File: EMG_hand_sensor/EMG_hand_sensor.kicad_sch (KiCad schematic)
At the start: 42 parts, among them J1 USB_C_Receptacle_USB2.0_16P, J2 Conn_01x04_Pin, SW1 SW_SPDT, U1 USBLC6-2SC6, U10 TRS_AUDIO_JACK_3.5mm, U11 TRS_AUDIO_JACK_3.5mm, U2 STM32F103C8Tx, U3 INA128, U4 TRS_AUDIO_JACK_3.5mm, U5 INA128, U6 INA128, U7 LT1762, U8 TRS_AUDIO_JACK_3.5mm, U9 INA128, Y1 16MHz

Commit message: new schematic done
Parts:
- C1, C12, C13, C14, C15, C2, C3, C4, C5, C6, C7, C8: footprint (none) -> Capacitor_SMD:C_0805_2012Metric_Pad1.18x1.45mm_HandSolder
- D1: footprint (none) -> Diode_SMD:D_0805_2012Metric
- FB1, R1, R10, R2, R3, R4, R5, R6, R7, R8, R9: footprint (none) -> Resistor_SMD:R_0805_2012Metric_Pad1.20x1.40mm_HandSolder
- J1: footprint (none) -> Connector_Molex:Molex_CLIK-Mate_502386-0970_1x09-1MP_P1.25mm_Horizontal
- J2: footprint (none) -> Connector_PinHeader_2.54mm:PinHeader_1x04_P2.54mm_Vertical
- SW1: footprint (none) -> Relay_THT:Relay_SPDT_Omron_G6E
- U3, U5, U6, U9: footprint (none) -> INA:SOIC127P600X175-8N
- Y1: footprint (none) -> Crystal:Crystal_SMD_3225-4Pin_3.2x2.5mm
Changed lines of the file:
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@@
 			)
 		)
-		(property "Footprint" ""
+		(property "Footprint" "Capacitor_SMD:C_0805_2012Metric_Pad1.18x1.45mm_HandSolder"
 			(at 48.26 64.77 0)
 			(effects
@@
 			)
 		)
-		(property "Footprint" ""
+		(property "Footprint" "Capacitor_SMD:C_0805_2012Metric_Pad1.18x1.45mm_HandSolder"
 			(at 125.73 62.23 0)
 			(effects
@@
 			)
 		)
-		(property "Footprint" ""
+		(property "Footprint" "INA:SOIC127P600X175-8N"
 			(at 160.02 30.48 0)
 			(effects
@@
 			)
 		)
-		(property "Footprint" ""
+		(property "Footprint" "Resistor_SMD:R_0805_2012Metric_Pad1.20x1.40mm_HandSolder"
 			(at 112.522 30.48 90)
 			(effects
@@
 			)
 		)
-		(property "Footprint" ""
+		(property "Footprint" "Capacitor_SMD:C_0805_2012Metric_Pad1.18x1.45mm_HandSolder"
 			(at 113.03 62.23 0)
 			(effects
@@
 			)
 		)
-		(property "Footprint" ""
+		(property "Footprint" "Relay_THT:Relay_SPDT_Omron_G6E"
 			(at 40.64 92.71 0)
 			(effects
@@
 			)
 		)
-		(property "Footprint" ""
+		(property "Footprint" "Crystal:Crystal_SMD_3225-4Pin_3.2x2.5mm"
 			(at 41.91 130.81 0)
 			(effects
@@
 			)
 		)
-		(property "Footprint" ""
+		(property "Footprint" "Capacitor_SMD:C_0805_2012Metric_Pad1.18x1.45mm_HandSolder"
 			(at 68.58 64.77 0)
 			(effects
@@
 			)
 		)
-		(property "Footprint" ""
+		(property "Footprint" "Capacitor_SMD:C_0805_2012Metric_Pad1.18x1.45mm_HandSolder"
 			(at 54.61 81.28 0)
 			(effects
@@
 			)
 		)
-		(property "Footprint" ""
+		(property "Footprint" "Resistor_SMD:R_0805_2012Metric_Pad1.20x1.40mm_HandSolder"
 			(at 129.032 165.1 90)
 			(effects
@@
 			)
 		)
-		(property "Footprint" ""
+		(property "Footprint" "Resistor_SMD:R_0805_2012Metric_Pad1.20x1.40mm_HandSolder"
 			(at 217.932 138.43 90)
 			(effects
@@
 			)
 		)
-		(property "Footprint" ""
+		(property "Footprint" "Resistor_SMD:R_0805_2012Metric_Pad1.20x1.40mm_HandSolder"
 			(at 272.542 105.41 90)
 			(effects
@@
 			)
 		)
-		(property "Footprint" ""
+		(property "Footprint" "INA:SOIC127P600X175-8N"
 			(at 158.75 57.15 0)
 			(effects
@@
 			)
 		)
-		(property "Footprint" ""
+		(property "Footprint" "Resistor_SMD:R_0805_2012Metric_Pad1.20x1.40mm_HandSolder"
 			(at 134.62 57.912 90)
 			(effects
@@
 			)
 		)
-		(property "Footprint" ""
+		(property "Footprint" "Diode_SMD:D_0805_2012Metric"
 			(at 267.97 101.6 0)
 			(effects
@@
 			)
 		)
-		(property "Footprint" ""
+		(property "Footprint" "Resistor_SMD:R_0805_2012Metric_Pad1.20x1.40mm_HandSolder"
 			(at 217.932 129.54 90)
 			(effects
@@
 			)
 		)
-		(property "Footprint" ""
+		(property "Footprint" "Capacitor_SMD:C_0805_2012Metric_Pad1.18x1.45mm_HandSolder"
 			(at 54.61 64.77 0)
 			(effects
@@
 			)
 		)
-		(property "Footprint" ""
+		(property "Footprint" "INA:SOIC127P600X175-8N"
 			(at 101.6 30.48 0)
 			(effects
@@
 			)
 		)
-		(property "Footprint" ""
+		(property "Footprint" "Capacitor_SMD:C_0805_2012Metric_Pad1.18x1.45mm_HandSolder"
 			(at 139.7 62.23 0)
 			(effects
@@
 			)
 		)
-		(property "Footprint" ""
+		(property "Footprint" "Connector_PinHeader_2.54mm:PinHeader_1x04_P2.54mm_Vertical"
 			(at 143.51 113.03 0)
 			(effects
@@
 			)
 		)
-		(property "Footprint" ""
+		(property "Footprint" "Resistor_SMD:R_0805_2012Metric_Pad1.20x1.40mm_HandSolder"
 			(at 169.672 57.15 90)
 			(effects
@@
 			)
 		)
-		(property "Footprint" ""
+		(property "Footprint" "Resistor_SMD:R_0805_2012Metric_Pad1.20x1.40mm_HandSolder"
 			(at 172.212 87.63 90)
 			(effects
@@
 			)
 		)
-		(property "Footprint" ""
+		(property "Footprint" "Connector_Molex:Molex_CLIK-Mate_502386-0970_1x09-1MP_P1.25mm_Horizontal"
 			(at 153.67 144.78 0)
 			(effects
@@
 			)
 		)
-		(property "Footprint" ""
+		(property "Footprint" "INA:SOIC127P600X175-8N"
 			(at 161.29 87.63 0)
 			(effects
@@
 			)
 		)
-		(property "Footprint" ""
+		(property "Footprint" "Resistor_SMD:R_0805_2012Metric_Pad1.20x1.40mm_HandSolder"
 			(at 135.382 165.1 90)
 			(effects
@@
 			)
 		)
-		(property "Footprint" ""
+		(property "Footprint" "Resistor_SMD:R_0805_2012Metric_Pad1.20x1.40mm_HandSolder"
 			(at 53.34 94.488 90)
 			(effects
@@
 			)
 		)
-		(property "Footprint" ""
+		(property "Footprint" "Capacitor_SMD:C_0805_2012Metric_Pad1.18x1.45mm_HandSolder"
 			(at 62.23 64.77 0)
 			(effects
@@
 			)
 		)
-		(property "Footprint" ""
+		(property "Footprint" "Resistor_SMD:R_0805_2012Metric_Pad1.20x1.40mm_HandSolder"
 			(at 170.942 30.48 90)
 			(effects
@@
 			)
 		)
-		(property "Footprint" ""
+		(property "Footprint" "Capacitor_SMD:C_0805_2012Metric_Pad1.18x1.45mm_HandSolder"
 			(at 39.37 64.77 0)
 			(effects
@@
 			)
 		)
-		(property "Footprint" ""
+		(property "Footprint" "Capacitor_SMD:C_0805_2012Metric_Pad1.18x1.45mm_HandSolder"
 			(at 74.93 64.77 0)
 			(effects
@@
 			)
 		)
-		(property "Footprint" ""
+		(property "Footprint" "Capacitor_SMD:C_0805_2012Metric_Pad1.18x1.45mm_HandSolder"
 			(at 53.34 135.89 0)
 			(effects
@@
 			)
 		)
-		(property "Footprint" ""
+		(property "Footprint" "Capacitor_SMD:C_0805_2012Metric_Pad1.18x1.45mm_HandSolder"
 			(at 29.21 137.16 0)
 			(effects

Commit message: starting pch layout
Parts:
- removed U10, U11, U4, U8: TRS_AUDIO_JACK_3.5mm, Connector_Audio:Jack_3.5mm_CUI_SJ-3523-SMT_Horizontal, symbol Audio_connector:TRS_connn
- added J3, J4, J5, J6: AudioJack3, Connector_Audio:Jack_3.5mm_CUI_SJ-3523-SMT_Horizontal, symbol Connector_Audio:AudioJack3
- J1: footprint Connector_Molex:Molex_CLIK-Mate_502386-0970_1x09-1MP_P1.25mm_Horizontal -> Connector_USB:USB_C_Receptacle_GCT_USB4105-xx-A_16P_TopMnt_Horizontal
- SW1: footprint Relay_THT:Relay_SPDT_Omron_G6E -> Button_Switch_SMD:SW_SPDT_CK_JS102011SAQN
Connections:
- net E1: now also J5.R; no longer U2.10 (PA0), U2.13 (PA3), U3.6
- net E2: now also J5.T
- net E3: now also J3.T; no longer U2.12 (PA2), U6.6
- net E4: now also J3.R; no longer U2.11 (PA1), U5.6, U9.6
- net E5: now also J6.R; no longer U5.3 (+)
- net E6: now also J6.T; no longer U5.2 (-)
- net E7: now also U5.3 (+), J4.T
- net E8: now also U5.2 (-), J4.R
- net GND: now also J3.S, J4.S, J5.S, J6.S
- new net O1: U2.10 (PA0), U6.6
- new net O2: U2.11 (PA1), U9.6
- new net O3: U2.12 (PA2), U5.6
- new net O4: U2.13 (PA3), U3.6

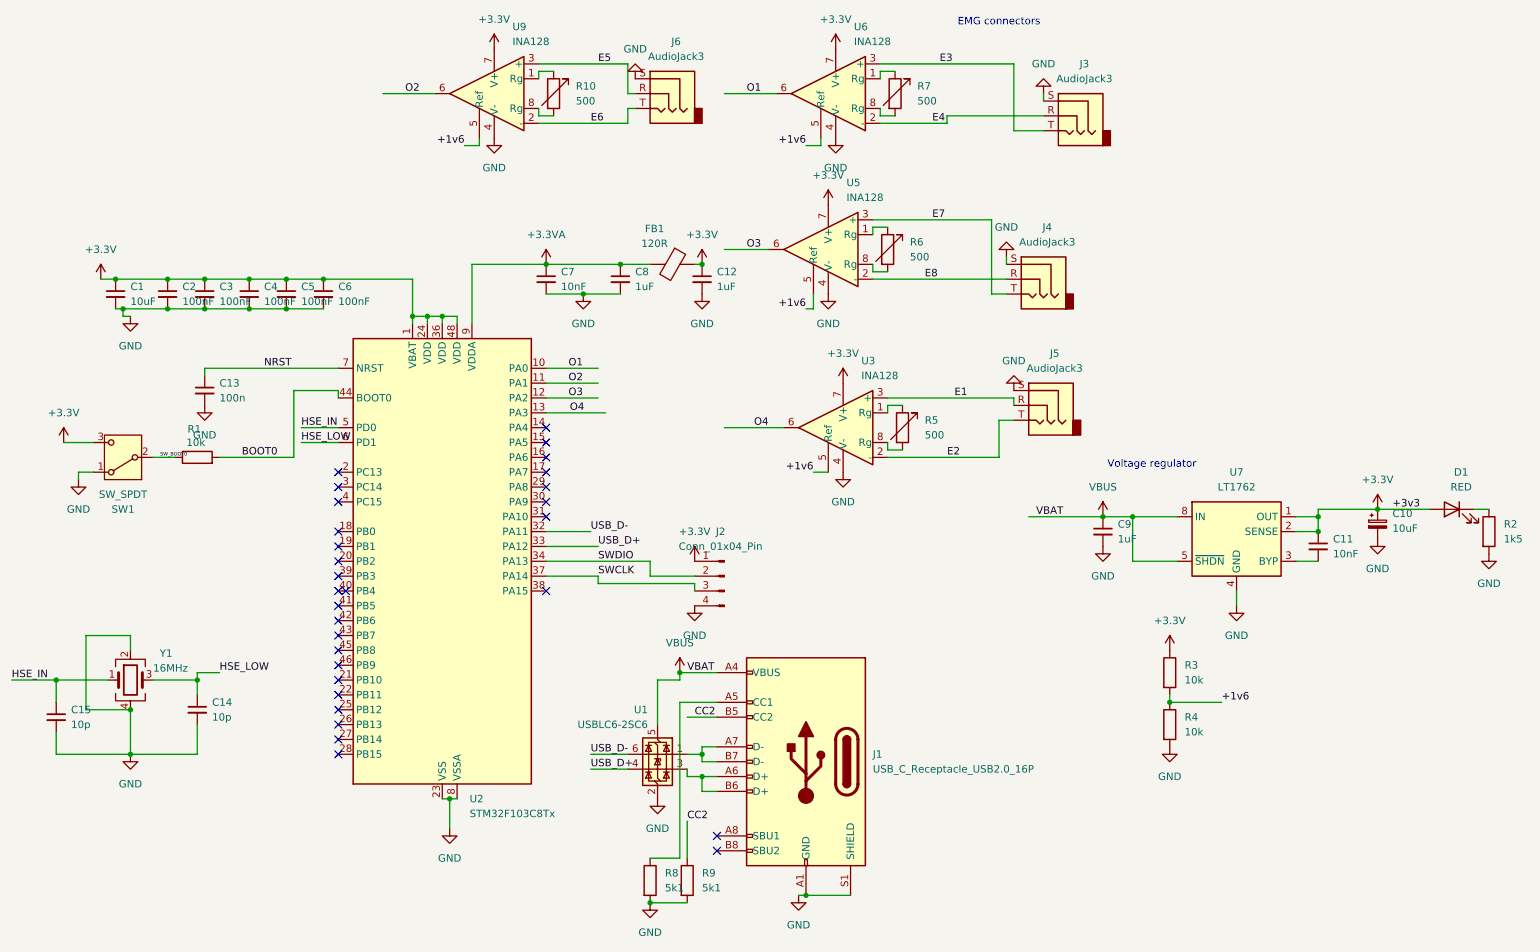
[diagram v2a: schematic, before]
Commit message: pcb layout finished
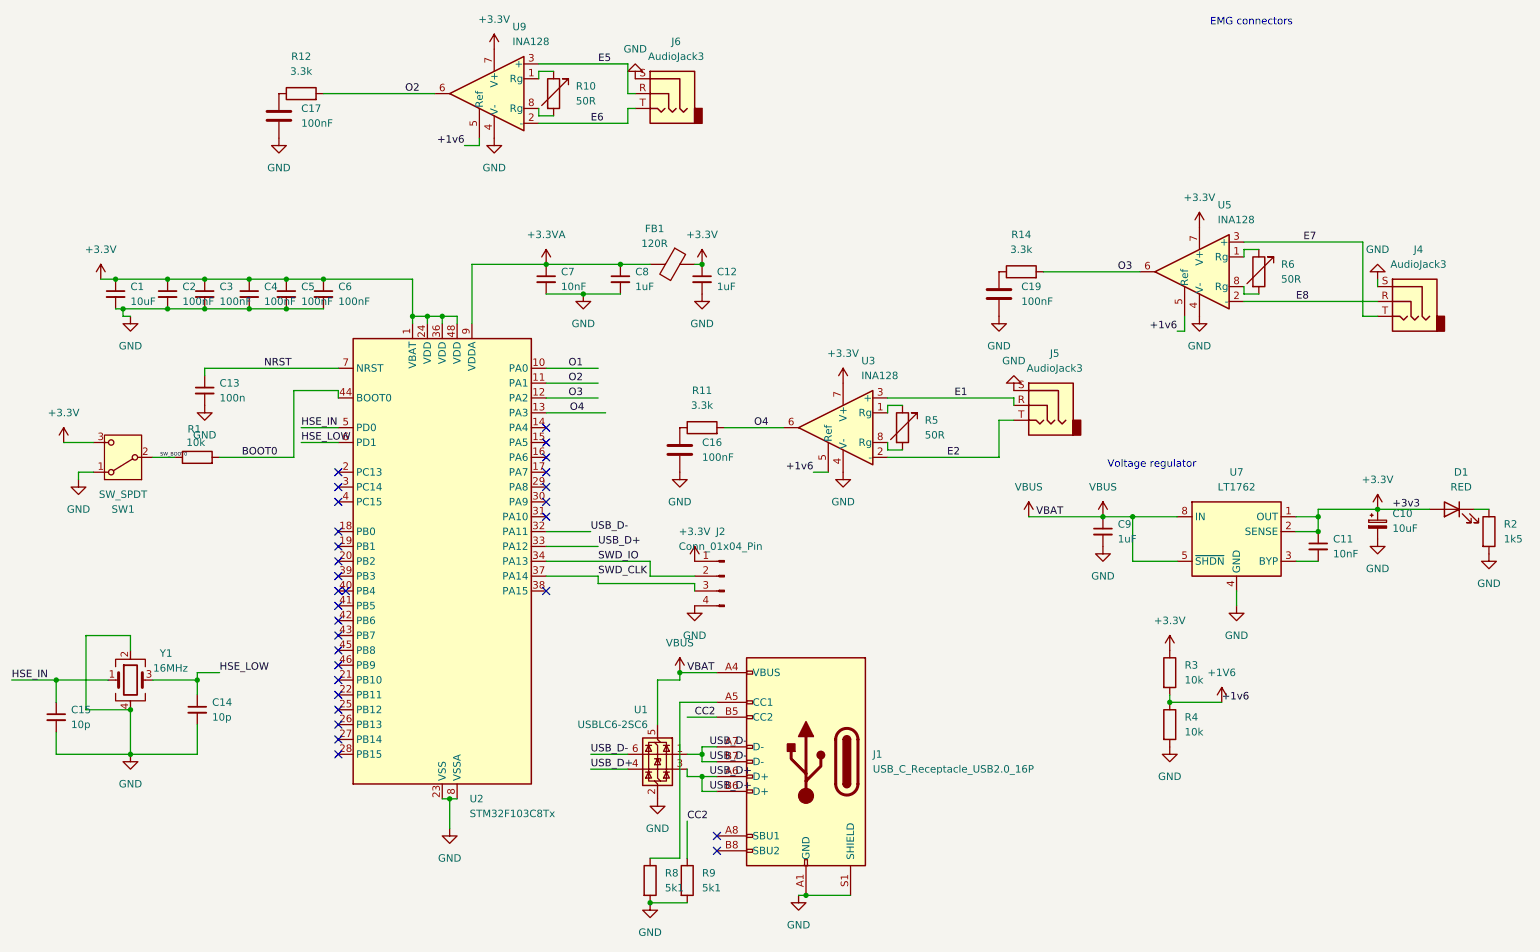
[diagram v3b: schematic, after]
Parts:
- removed J3: AudioJack3, Connector_Audio:Jack_3.5mm_CUI_SJ-3523-SMT_Horizontal, symbol Connector_Audio:AudioJack3
- removed R7: 500, Resistor_SMD:R_0805_2012Metric_Pad1.20x1.40mm_HandSolder, symbol Device:R_Variable
- removed U6: INA128, INA:SOIC127P600X175-8N, symbol Amplifier_Instrumentation:INA128
- added C16, C17, C19: 100nF, Capacitor_SMD:C_0805_2012Metric_Pad1.18x1.45mm_HandSolder, symbol Device:C
- added R11, R12, R14: 3.3k, Resistor_SMD:R_0805_2012Metric_Pad1.20x1.40mm_HandSolder, symbol Device:R
- R10, R5, R6: value 500 -> 50R
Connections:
- net GND: now also C16.2, C17.2, C19.2
- net O2: now also R12.2
- net O3: now also R14.2
- net O4: now also R11.2
- net USB_D+: now also J1.A6 (D+), J1.B6 (D+), U1.3 (I/O2)
- net USB_D-: now also J1.A7 (D-), J1.B7 (D-), U1.1 (I/O1)
- net +1v6 renamed +1V6
- net SWCLK renamed SWD_CLK
- net SWDIO renamed SWD_IO
- new net: C19.1, R14.1
- new net: C17.1, R12.1
- new net: C16.1, R11.1
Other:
- moved on the sheet: J4, R6, U5

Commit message: routing time
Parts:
- added H1, H2: MountingHole_Pad, symbol Mechanical:MountingHole_Pad
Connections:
- net GND: now also H1.1, H2.1

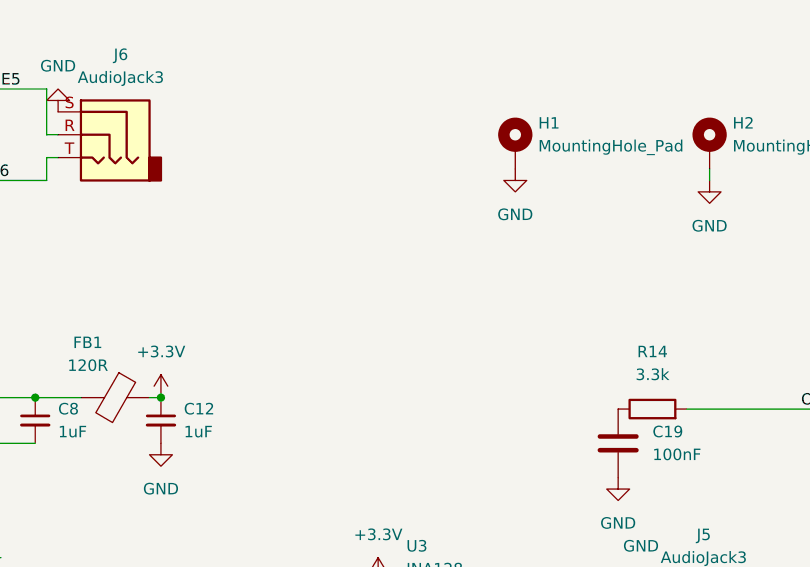
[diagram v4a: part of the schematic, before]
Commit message: Need to add guard traces and vias and then I can start routing
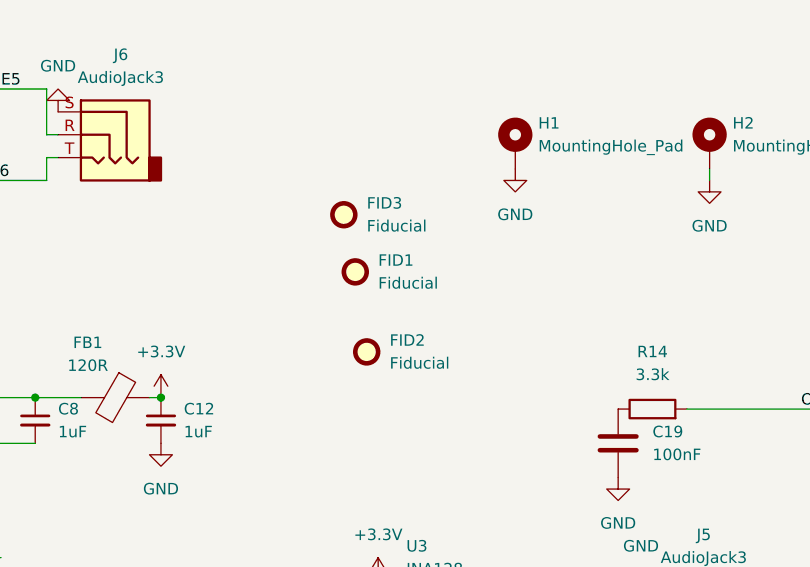
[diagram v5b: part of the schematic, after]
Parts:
- added FID1, FID2, FID3: Fiducial, Fiducial:Fiducial_0.5mm_Mask2mm, symbol Mechanical:Fiducial
- H1, H2: footprint (none) -> MountingHole:MountingHole_2.2mm_M2_Pad
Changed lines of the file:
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@@
+	)
+	(symbol
+		(lib_id "Mechanical:Fiducial")
+		(at 160.02 39.37 0)
+		(unit 1)
+		(exclude_from_sim no)
+		(in_bom no)
+		(on_board yes)
+		(dnp no)
+		(fields_autoplaced yes)
+		(property "Reference" "FID3"
+			(at 162.56 38.0999 0)
+			(effects
+				(font
+					(size 1.27 1.27)
+				)
+				(justify left)
+			)
+		)
+		(property "Value" "Fiducial"
+			(at 162.56 40.6399 0)
+			(effects
+				(font
+					(size 1.27 1.27)
+				)
+				(justify left)
+			)
+		)
+		(property "Footprint" "Fiducial:Fiducial_0.5mm_Mask2mm"
+			(at 160.02 39.37 0)
+			(effects
+				(font
+					(size 1.27 1.27)
+				)
+				(hide yes)
+			)
+		)
+		(property "Datasheet" "~"
+			(at 160.02 39.37 0)
+			(effects
+				(font
+					(size 1.27 1.27)
+				)
+				(hide yes)
+			)
+		)
+		(property "Description" "Fiducial Marker"
+			(at 160.02 39.37 0)
+			(effects
+				(font
+					(size 1.27 1.27)
+				)
+				(hide yes)
+			)
+		)
+		(instances
+			(project "EMG_hand_sensor"
+				(path "/84a42da6-643f-42bf-9876-7927dca3da2c"
+					(reference "FID3")
+					(unit 1)
+				)
+			)
+		)
 	)
 	(symbol
@@
 				(path "/84a42da6-643f-42bf-9876-7927dca3da2c"
 					(reference "C8")
+					(unit 1)
+				)
+			)
+		)
+	)
+	(symbol
+		(lib_id "Mechanical:Fiducial")
+		(at 161.29 45.72 0)
+		(unit 1)
+		(exclude_from_sim no)
+		(in_bom no)
+		(on_board yes)
+		(dnp no)
+		(fields_autoplaced yes)
+		(property "Reference" "FID1"
+			(at 163.83 44.4499 0)
+			(effects
+				(font
+					(size 1.27 1.27)
+				)
+				(justify left)
+			)
+		)
+		(property "Value" "Fiducial"
+			(at 163.83 46.9899 0)
+			(effects
+				(font
+					(size 1.27 1.27)
+				)
+				(justify left)
+			)
+		)
+		(property "Footprint" "Fiducial:Fiducial_0.5mm_Mask2mm"
+			(at 161.29 45.72 0)
+			(effects
+				(font
+					(size 1.27 1.27)
+				)
+				(hide yes)
+			)
+		)
+		(property "Datasheet" "~"
+			(at 161.29 45.72 0)
+			(effects
+				(font
+					(size 1.27 1.27)
+				)
+				(hide yes)
+			)
+		)
+		(property "Description" "Fiducial Marker"
+			(at 161.29 45.72 0)
+			(effects
+				(font
+					(size 1.27 1.27)
+				)
+				(hide yes)
+			)
+		)
+		(instances
+			(project ""
+				(path "/84a42da6-643f-42bf-9876-7927dca3da2c"
+					(reference "FID1")
 					(unit 1)
 				)
@@
 			)
 		)
-		(property "Footprint" ""
+		(property "Footprint" "MountingHole:MountingHole_2.2mm_M2_Pad"
 			(at 200.66 31.75 0)
 			(effects
@@
 	)
 	(symbol
+		(lib_id "Mechanical:Fiducial")
+		(at 162.56 54.61 0)
+		(unit 1)
+		(exclude_from_sim no)
+		(in_bom no)
+		(on_board yes)
+		(dnp no)
+		(fields_autoplaced yes)
+		(property "Reference" "FID2"
+			(at 165.1 53.3399 0)
+			(effects
+				(font
+					(size 1.27 1.27)
+				)
+				(justify left)
+			)
+		)
+		(property "Value" "Fiducial"
+			(at 165.1 55.8799 0)
+			(effects
+				(font
+					(size 1.27 1.27)
+				)
+				(justify left)
+			)
+		)
+		(property "Footprint" "Fiducial:Fiducial_0.5mm_Mask2mm"
+			(at 162.56 54.61 0)
+			(effects
+				(font
+					(size 1.27 1.27)
+				)
+				(hide yes)
+			)
+		)
+		(property "Datasheet" "~"
+			(at 162.56 54.61 0)
+			(effects
+				(font
+					(size 1.27 1.27)
+				)
+				(hide yes)
+			)
+		)
+		(property "Description" "Fiducial Marker"
+			(at 162.56 54.61 0)
+			(effects
+				(font
+					(size 1.27 1.27)
+				)
+				(hide yes)
+			)
+		)
+		(instances
+			(project ""
+				(path "/84a42da6-643f-42bf-9876-7927dca3da2c"
+					(reference "FID2")
+					(unit 1)
+				)
+			)
+		)
+	)
+	(symbol
 		(lib_id "power:+5V")
 		(at 195.58 102.87 0)
@@
 			)
 		)
-		(property "Footprint" ""
+		(property "Footprint" "MountingHole:MountingHole_2.2mm_M2_Pad"
 			(at 179.07 31.75 0)
 			(effects

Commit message: done with most of the routing
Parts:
- removed R10, R5, R6: 50R, Resistor_SMD:R_0805_2012Metric_Pad1.20x1.40mm_HandSolder, symbol Device:R_Variable
- added C18, C20, C21: 100nF, Capacitor_SMD:C_0805_2012Metric_Pad1.18x1.45mm_HandSolder, symbol Device:C_Small
- added RV1, RV2, RV3: 500R, Potentiometer_SMD:Potentiometer_Bourns_3214W_Vertical, symbol Device:R_Potentiometer
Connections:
- net +3.3V: now also C18.1, C20.1, C21.1
- net GND: now also C18.2, C20.2, C21.2
- net RV3_1: now reaches U9.1 (Rg)
- net RV3_1: now also RV3.1, RV3.2
- net RV3_3: now reaches U9.8 (Rg)
- net RV3_3: now also RV3.3
- net at U5.1 (Rg): now also RV2.1, RV2.2
- net at U5.8 (Rg): now also RV2.3
- net at U3.1 (Rg): now also RV1.1, RV1.2
- net at U3.8 (Rg): now also RV1.3
- net O1: no longer names the net of U2.10 (PA0)
- no-connect marks 30 -> 31
